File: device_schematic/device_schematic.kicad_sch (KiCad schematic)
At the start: 1 part

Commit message: Device schematic update
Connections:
- net signal processing/NUCLEO 3V3: now reaches U?.16 (+3V3)
- net USB-C connector/NUCLEO PA11 renamed USB-C connector/NUCLEO USB_DM
- net USB-C connector/NUCLEO PA12 renamed USB-C connector/NUCLEO USB_DP
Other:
- added sheet signal processing1 (signal_processing.kicad_sch)
- sheet USB-C connector ports: added NUCLEO USB_DM, NUCLEO USB_DP; removed NUCLEO PA11, NUCLEO PA12, USB 5V
- sheet signal processing ports: added -5V, NUCLEO 3V3, NUCLEO 5V, NUCLEO ADC, NUCLEO CHANNEL ENABLED; removed none

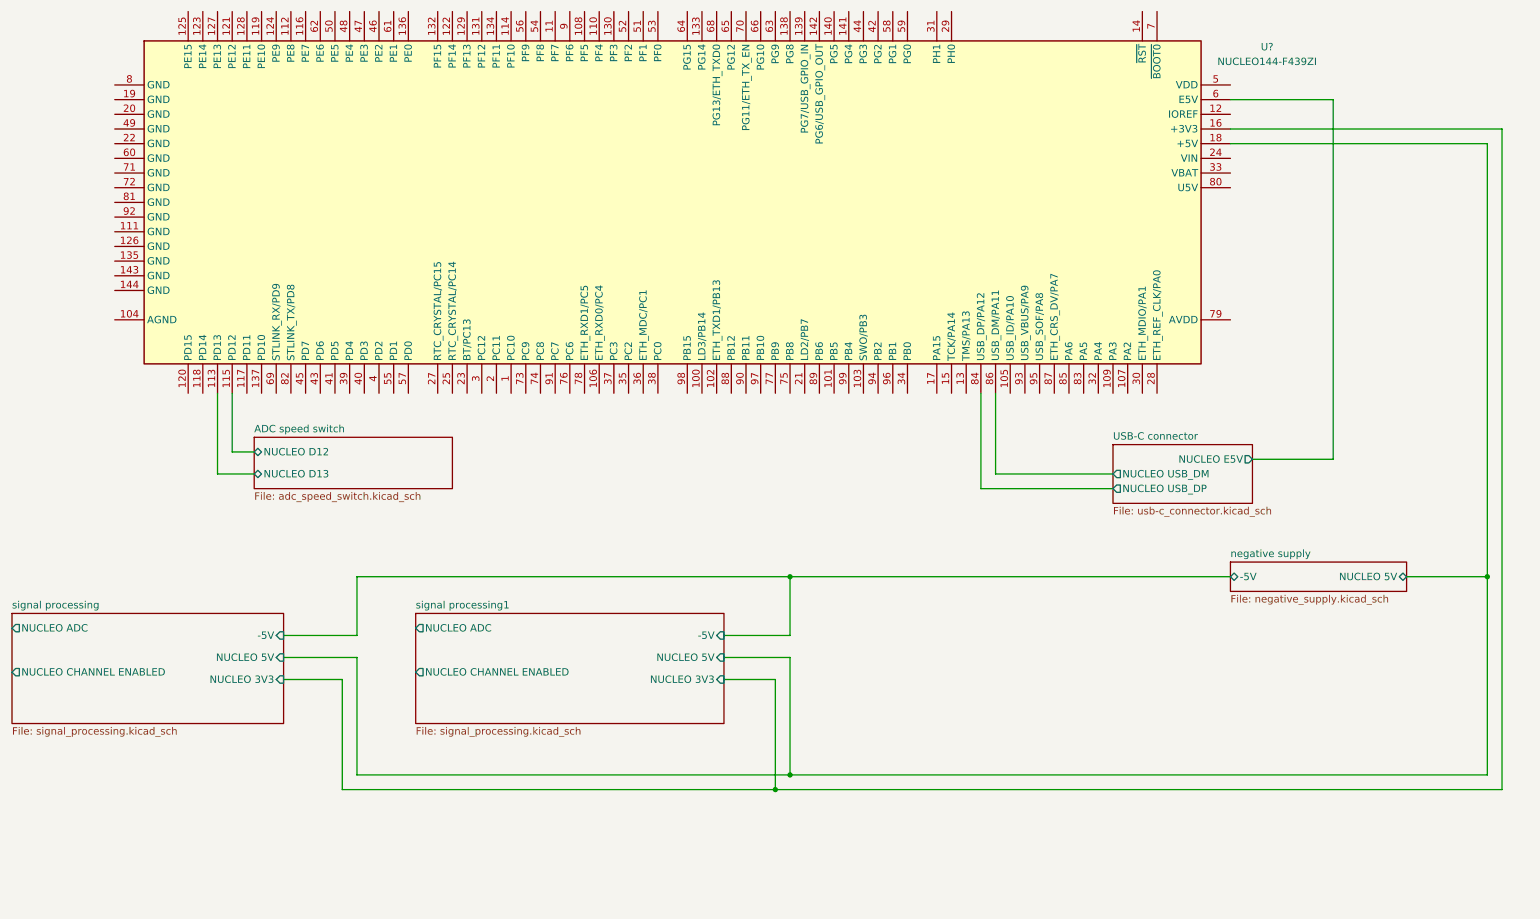
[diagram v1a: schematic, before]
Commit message: Device schematic finished version
+ correction to use D7 in place of D13
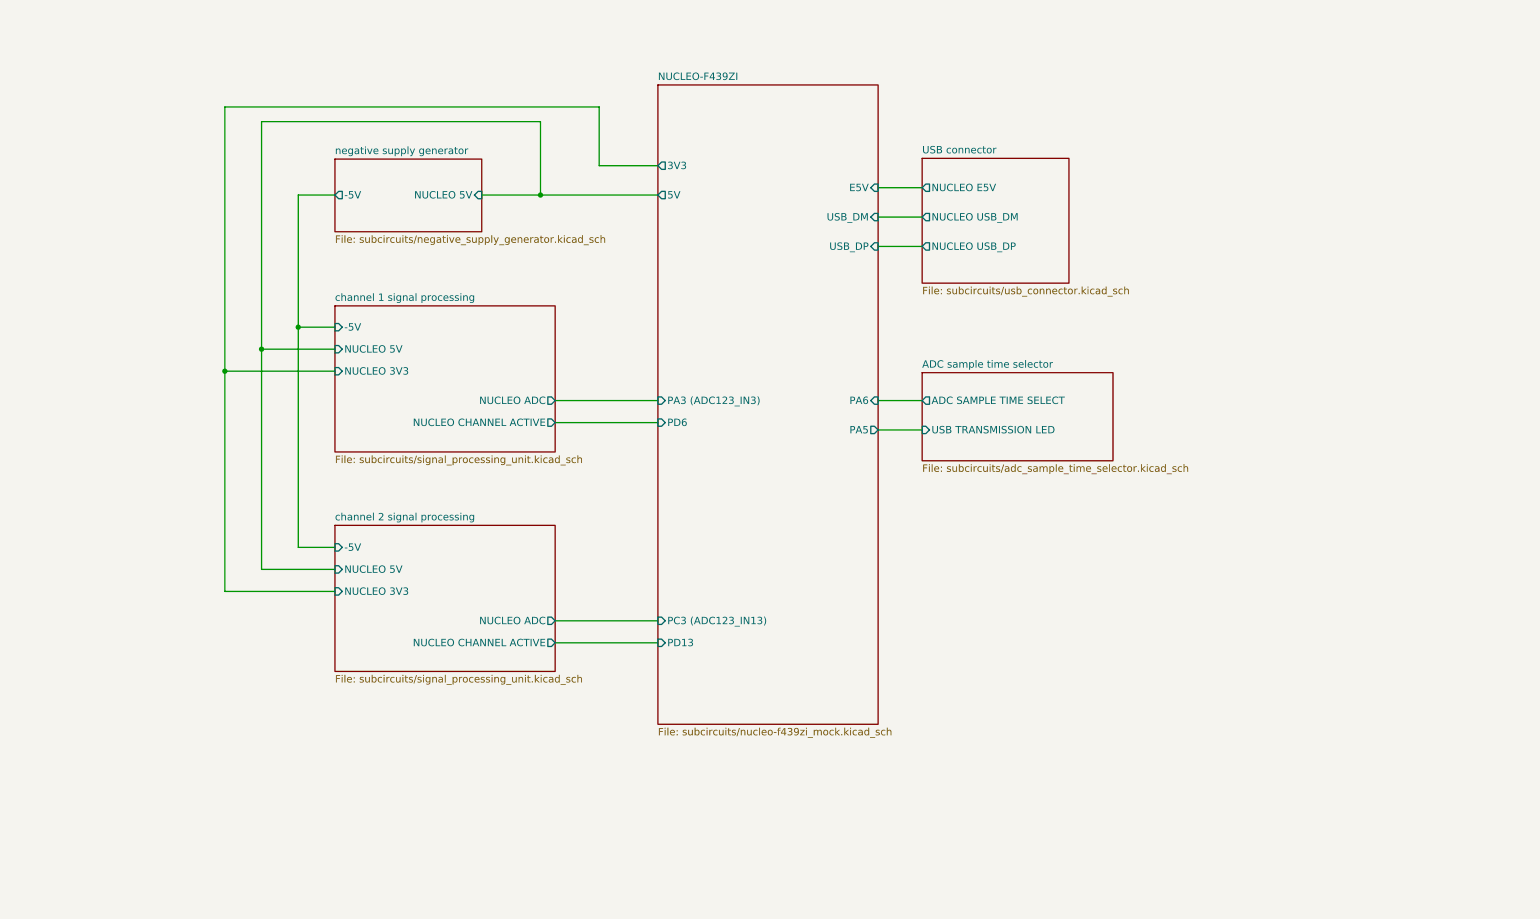
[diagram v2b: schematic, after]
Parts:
- removed U?: NUCLEO144-F439ZI, Module:ST_Morpho_Connector_144_STLink, symbol MCU_Module:NUCLEO144-F439ZI
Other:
- sheet ADC speed switch renamed ADC sample time selector
- sheet USB-C connector renamed USB connector
- sheet negative supply renamed negative supply generator
- sheet signal processing renamed channel 1 signal processing
- removed sheet signal processing1
- added sheet NUCLEO-F439ZI (subcircuits/nucleo-f439zi_mock.kicad_sch)
- added sheet channel 2 signal processing (subcircuits/signal_processing_unit.kicad_sch)
- sheet ADC sample time selector: file adc_speed_switch.kicad_sch -> subcircuits/adc_sample_time_selector.kicad_sch
- sheet ADC sample time selector ports: added ADC SAMPLE TIME SELECT, USB TRANSMISSION LED; removed NUCLEO D12, NUCLEO D13
- sheet USB connector: file usb-c_connector.kicad_sch -> subcircuits/usb_connector.kicad_sch
- sheet channel 1 signal processing: file signal_processing.kicad_sch -> subcircuits/signal_processing_unit.kicad_sch
- sheet channel 1 signal processing ports: added NUCLEO CHANNEL ACTIVE; removed NUCLEO CHANNEL ENABLED
- sheet negative supply generator: file negative_supply.kicad_sch -> subcircuits/negative_supply_generator.kicad_sch
